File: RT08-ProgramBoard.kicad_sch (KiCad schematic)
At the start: 5 parts, among them J1 PWR/Addr, J2 Instruction, J3 Data, J4 Instruction, J5 Data

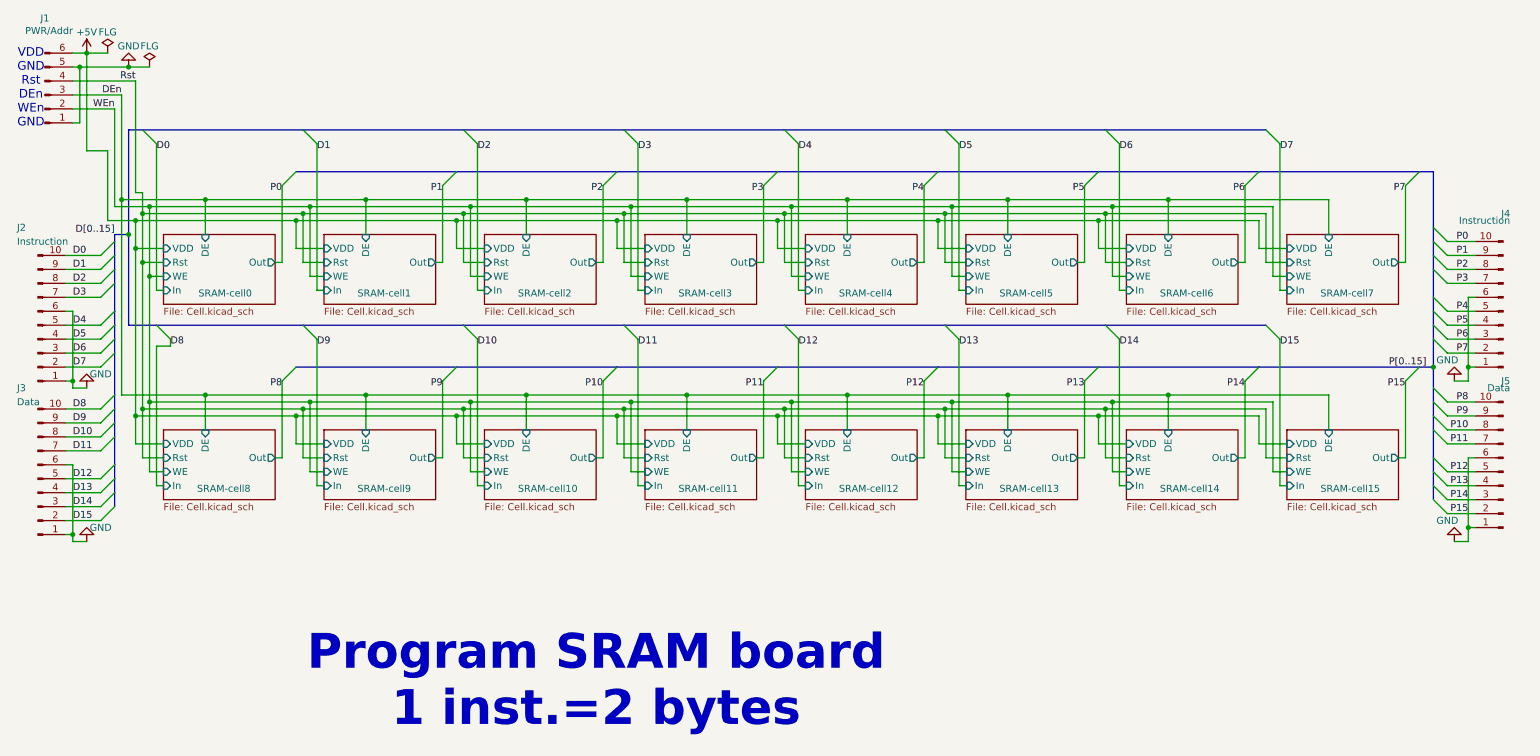
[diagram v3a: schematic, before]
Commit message: Deleted '-' from its name, officially
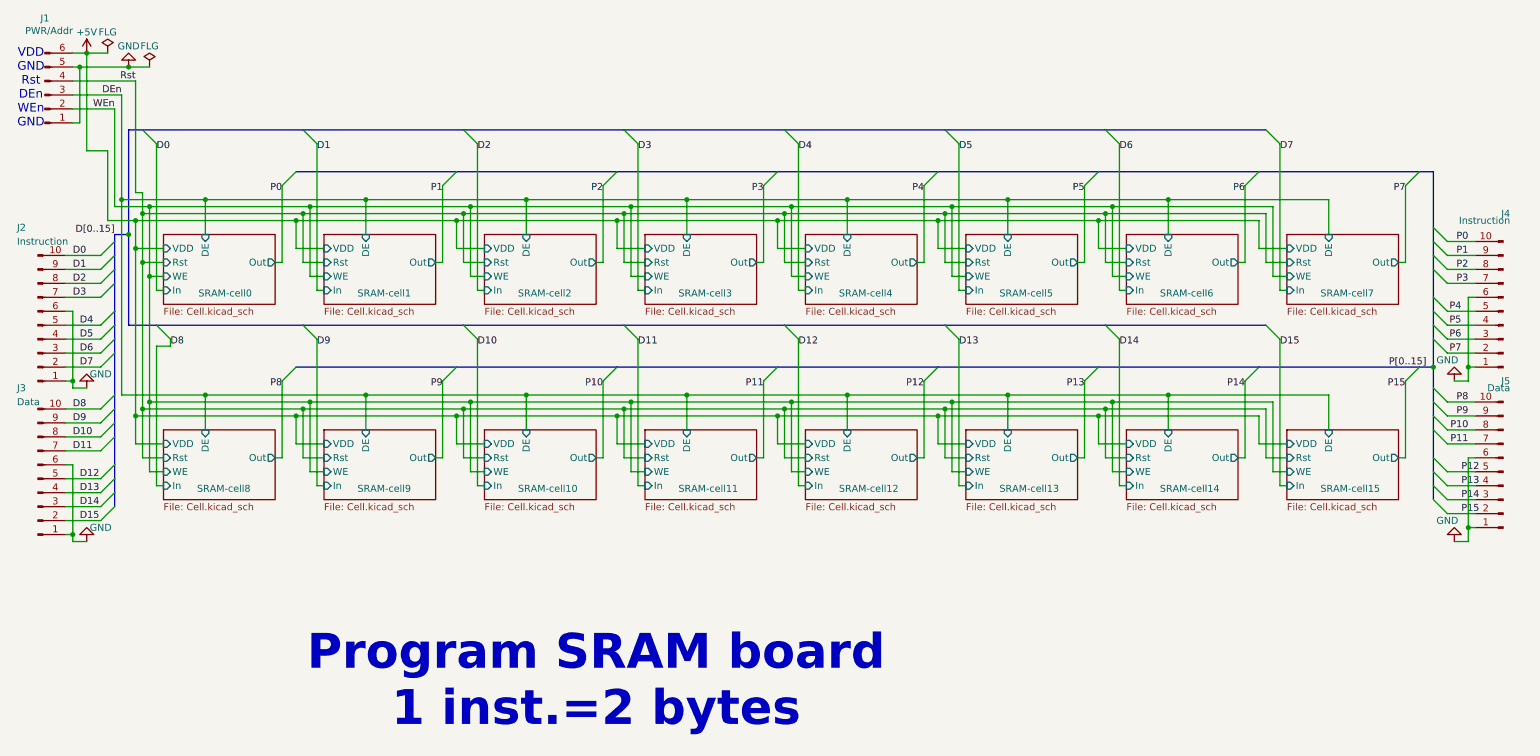
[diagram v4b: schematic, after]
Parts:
- J5: footprint Connector_PinHeader_2.54mm:PinHeader_1x08_P2.54mm_Horizontal -> Connector_PinHeader_2.54mm:PinHeader_1x10_P2.54mm_Horizontal
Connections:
- net GND: no longer J2.2 (Pin_2), J2.3 (Pin_3), J2.4 (Pin_4), J2.5 (Pin_5), J3.2 (Pin_2), J3.3 (Pin_3), J3.4 (Pin_4), J3.5 (Pin_5), J4.2 (Pin_2), J4.3 (Pin_3), J4.4 (Pin_4), J4.5 (Pin_5), J5.2 (Pin_2), J5.3 (Pin_3), J5.4 (Pin_4), J5.5 (Pin_5)
- new net D12: J3.5 (Pin_5)
- new net D13: J3.4 (Pin_4)
- new net D14: J3.3 (Pin_3)
- new net D15: J3.2 (Pin_2)
- new net D4: J2.5 (Pin_5)
- new net D5: J2.4 (Pin_4)
- new net D6: J2.3 (Pin_3)
- new net D7: J2.2 (Pin_2)
- new net P12: J5.5 (Pin_5)
- new net P13: J5.4 (Pin_4)
- new net P14: J5.3 (Pin_3)
- new net P15: J5.2 (Pin_2)
- new net P4: J4.5 (Pin_5)
- new net P5: J4.4 (Pin_4)
- new net P6: J4.3 (Pin_3)
- new net P7: J4.2 (Pin_2)
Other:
- title: Y-tran RT-08 Program board -> Y-tran RT08 Program board
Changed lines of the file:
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@@
 	(paper "A4")
 	(title_block
-		(title "Y-tran RT-08 Program board")
+		(title "Y-tran RT08 Program board")
 		(date "2025/3~5")
 		(rev "C")
@@
 		)
 	)
-	(wire
-		(pts
-			(xy 21.59 120.65) (xy 27.94 120.65)
-		)
-		(stroke
-			(width 0)
-			(type default)
-		)
-	)
 	(bus
 		(pts
@@
 	(wire
 		(pts
+			(xy 273.05 154.94) (xy 278.13 154.94)
+		)
+		(stroke
+			(width 0)
+			(type default)
+		)
+	)
+	(wire
+		(pts
 			(xy 66.04 134.62) (xy 95.25 134.62)
 		)
@@
 	(wire
 		(pts
+			(xy 273.05 120.65) (xy 278.13 120.65)
+		)
+		(stroke
+			(width 0)
+			(type default)
+		)
+	)
+	(wire
+		(pts
 			(xy 93.98 135.89) (xy 93.98 144.78)
 		)
@@
 	(wire
 		(pts
+			(xy 22.86 146.05) (xy 22.86 158.75)
+		)
+		(stroke
+			(width 0)
+			(type default)
+		)
+	)
+	(wire
+		(pts
 			(xy 123.19 144.78) (xy 127 144.78)
 		)
@@
 		)
 	)
+	(wire
+		(pts
+			(xy 276.86 144.78) (xy 276.86 157.48)
+		)
+		(stroke
+			(width 0)
+			(type default)
+		)
+	)
 	(bus
 		(pts
@@
 	(wire
 		(pts
-			(xy 21.59 123.19) (xy 27.94 123.19)
-		)
-		(stroke
-			(width 0)
-			(type default)
-		)
-	)
-	(wire
-		(pts
 			(xy 134.62 97.79) (xy 163.83 97.79)
 		)
@@
 	(wire
 		(pts
-			(xy 22.86 146.05) (xy 22.86 158.75)
-		)
-		(stroke
-			(width 0)
-			(type default)
-		)
-	)
-	(wire
-		(pts
 			(xy 205.74 144.78) (xy 207.01 144.78)
 		)
@@
 	(wire
 		(pts
+			(xy 276.86 115.57) (xy 276.86 128.27)
+		)
+		(stroke
+			(width 0)
+			(type default)
+		)
+	)
+	(wire
+		(pts
 			(xy 22.86 83.82) (xy 24.13 83.82)
 		)
@@
 	(wire
 		(pts
+			(xy 21.59 123.19) (xy 27.94 123.19)
+		)
+		(stroke
+			(width 0)
+			(type default)
+		)
+	)
+	(wire
+		(pts
 			(xy 36.83 111.76) (xy 36.83 134.62)
 		)
@@
 	(wire
 		(pts
-			(xy 273.05 154.94) (xy 278.13 154.94)
-		)
-		(stroke
-			(width 0)
-			(type default)
-		)
-	)
-	(wire
-		(pts
 			(xy 21.59 140.97) (xy 27.94 140.97)
 		)
@@
 	(wire
 		(pts
-			(xy 276.86 115.57) (xy 276.86 128.27)
-		)
-		(stroke
-			(width 0)
-			(type default)
-		)
-	)
-	(wire
-		(pts
 			(xy 147.32 109.22) (xy 148.59 109.22)
 		)
@@
 	(wire
 		(pts
-			(xy 181.61 100.33) (xy 210.82 100.33)
+			(xy 22.86 118.11) (xy 22.86 130.81)
 		)
 		(stroke
@@
 	(wire
 		(pts
-			(xy 105.41 97.79) (xy 105.41 104.14)
+			(xy 181.61 100.33) (xy 210.82 100.33)
 		)
 		(stroke
@@
 	(wire
 		(pts
-			(xy 210.82 100.33) (xy 210.82 109.22)
+			(xy 105.41 97.79) (xy 105.41 104.14)
 		)
 		(stroke
@@
 	(wire
 		(pts
-			(xy 63.5 142.24) (xy 68.58 142.24)
+			(xy 210.82 100.33) (xy 210.82 109.22)
 		)
 		(stroke
@@
 	(wire
 		(pts
-			(xy 21.59 151.13) (xy 27.94 151.13)
+			(xy 63.5 142.24) (xy 68.58 142.24)
 		)
 		(stroke
@@
 	(wire
 		(pts
+			(xy 21.59 151.13) (xy 27.94 151.13)
+		)
+		(stroke
+			(width 0)
+			(type default)
+		)
+	)
+	(wire
+		(pts
 			(xy 240.03 144.78) (xy 243.84 144.78)
 		)
@@
 	(wire
 		(pts
+			(xy 21.59 128.27) (xy 27.94 128.27)
+		)
+		(stroke
+			(width 0)
+			(type default)
+		)
+	)
+	(wire
+		(pts
 			(xy 163.83 97.79) (xy 163.83 104.14)
 		)
@@
 	(wire
 		(pts
-			(xy 21.59 128.27) (xy 27.94 128.27)
+			(xy 34.29 142.24) (xy 39.37 142.24)
 		)
 		(stroke
@@
 	(wire
 		(pts
-			(xy 34.29 142.24) (xy 39.37 142.24)
+			(xy 21.59 125.73) (xy 27.94 125.73)
 		)
 		(stroke
@@
 	(wire
 		(pts
-			(xy 273.05 137.16) (xy 278.13 137.16)
+			(xy 21.59 120.65) (xy 27.94 120.65)
 		)
 		(stroke
@@
 	(wire
 		(pts
-			(xy 30.48 81.28) (xy 30.48 99.06)
+			(xy 273.05 137.16) (xy 278.13 137.16)
 		)
 		(stroke
@@
 		)
 	)
-	(bus
+	(wire
 		(pts
-			(xy 30.48 140.97) (xy 30.48 146.05)
+			(xy 30.48 81.28) (xy 30.48 99.06)
 		)
 		(stroke
@@
 		)
 	)
-	(wire
+	(bus
 		(pts
-			(xy 21.59 125.73) (xy 27.94 125.73)
+			(xy 30.48 140.97) (xy 30.48 146.05)
 		)
 		(stroke
@@
 		)
 	)
-	(wire
-		(pts
-			(xy 273.05 120.65) (xy 278.13 120.65)
-		)
-		(stroke
-			(width 0)
-			(type default)
-		)
-	)
 	(bus
 		(pts
@@
 	(wire
 		(pts
-			(xy 22.86 118.11) (xy 22.86 130.81)
-		)
-		(stroke
-			(width 0)
-			(type default)
-		)
-	)
-	(wire
-		(pts
-			(xy 276.86 144.78) (xy 276.86 157.48)
-		)
-		(stroke
-			(width 0)
-			(type default)
-		)
-	)
-	(wire
-		(pts
 			(xy 92.71 106.68) (xy 97.79 106.68)
 		)
@@
 	)
 	(label "D14"
-		(at 22.86 153.67 0)
+		(at 24.13 153.67 0)
 		(effects
 			(font
@@
 	)
 	(label "D15"
-		(at 22.86 156.21 0)
+		(at 24.13 156.21 0)
 		(effects
 			(font
@@
 	)
 	(label "P12"
-		(at 276.86 147.32 180)
+		(at 275.59 147.32 0)
 		(effects
 			(font
 				(size 1.27 1.27)
 			)
-			(justify right bottom)
+			(justify left bottom)
 		)
 	)
@@
 	)
 	(label "P7"
-		(at 276.86 125.73 180)
+		(at 275.59 125.73 180)
 		(effects
 			(font
@@
 	)
 	(label "D4"
-		(at 22.86 120.65 0)
+		(at 24.13 120.65 0)
 		(effects
 			(font
@@
 	)
 	(label "D5"
-		(at 22.86 123.19 0)
+		(at 24.13 123.19 0)
 		(effects
 			(font
@@
 	)
 	(label "D7"
-		(at 22.86 128.27 0)
+		(at 24.13 128.27 0)
 		(effects
 			(font
@@
 	)
 	(label "D13"
-		(at 22.86 151.13 0)
+		(at 24.13 151.13 0)
 		(effects
 			(font
@@
 	)
 	(label "P6"
-		(at 276.86 123.19 180)
+		(at 275.59 123.19 180)
 		(effects
 			(font
@@
 	)
 	(label "P15"
-		(at 276.86 154.94 180)
+		(at 275.59 154.94 0)
 		(effects
 			(font
 				(size 1.27 1.27)
 			)
-			(justify right bottom)
+			(justify left bottom)
 		)
 	)
 	(label "P4"
-		(at 276.86 118.11 180)
+		(at 275.59 118.11 180)
 		(effects
 			(font
@@
 	)
 	(label "P14"
-		(at 276.86 152.4 180)
+		(at 275.59 152.4 0)
 		(effects
 			(font
 				(size 1.27 1.27)
 			)
-			(justify right bottom)
+			(justify left bottom)
 		)
 	)
@@
 	)
 	(label "D6"
-		(at 22.86 125.73 0)
+		(at 24.13 125.73 0)
 		(effects
 			(font
@@
 	)
 	(label "P5"
-		(at 276.86 120.65 180)
+		(at 275.59 120.65 180)
 		(effects
 			(font
@@
 	)
 	(label "D12"
-		(at 22.86 148.59 0)
+		(at 24.13 148.59 0)
 		(effects
 			(font
@@
 	)
 	(label "P13"
-		(at 276.86 149.86 180)
+		(at 275.59 149.86 0)
 		(effects
 			(font
 				(size 1.27 1.27)
 			)
-			(justify right bottom)
+			(justify left bottom)
 		)
 	)
@@
 			)
 		)
-		(property "Footprint" "Connector_PinHeader_2.54mm:PinHeader_1x08_P2.54mm_Horizontal"
+		(property "Footprint" "Connector_PinHeader_2.54mm:PinHeader_1x10_P2.54mm_Horizontal"
 			(at 283.21 147.32 0)
 			(effects

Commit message: Updated pinouts n' something
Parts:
- removed J3, J5: Data, Connector_PinHeader_2.54mm:PinHeader_1x10_P2.54mm_Horizontal, symbol Connector:Conn_01x10_Pin
- removed J4: Instruction, Connector_PinHeader_2.54mm:PinHeader_1x10_P2.54mm_Horizontal, symbol Connector:Conn_01x10_Pin
- added J3, J7: Inst-2, Connector_PinHeader_2.54mm:PinHeader_1x06_P2.54mm_Horizontal, symbol Connector:Conn_01x06_Pin
- added J4, J8: Data-1, Connector_PinHeader_2.54mm:PinHeader_1x06_P2.54mm_Horizontal, symbol Connector:Conn_01x06_Pin
- added J5, J9: Data-2, Connector_PinHeader_2.54mm:PinHeader_1x06_P2.54mm_Horizontal, symbol Connector:Conn_01x06_Pin
- added J6: Inst-1, Connector_PinHeader_2.54mm:PinHeader_1x06_P2.54mm_Horizontal, symbol Connector:Conn_01x06_Pin
- J2: value Instruction -> Inst-1; footprint Connector_PinHeader_2.54mm:PinHeader_1x10_P2.54mm_Horizontal -> Connector_PinHeader_2.54mm:PinHeader_1x06_P2.54mm_Horizontal; symbol Connector:Conn_01x10_Pin -> Connector:Conn_01x06_Pin
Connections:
- net D0: now also J2.6 (Pin_6); no longer J2.10 (Pin_10)
- net D1: now also J2.5 (Pin_5); no longer J2.9 (Pin_9)
- net D10: now also J4.3 (Pin_3)
- net D11: now also J4.2 (Pin_2)
- net D12: now also J5.6 (Pin_6)
- net D13: now also J5.5 (Pin_5)
- net D14: now also J5.3 (Pin_3)
- net D15: now also J5.2 (Pin_2)
- net D2: now also J2.3 (Pin_3); no longer J2.8 (Pin_8)
- net D3: now also J2.2 (Pin_2); no longer J2.7 (Pin_7)
- net D4: now also J3.6 (Pin_6); no longer J2.5 (Pin_5)
- net D5: now also J3.5 (Pin_5); no longer J2.4 (Pin_4)
- net D6: now also J3.3 (Pin_3); no longer J2.3 (Pin_3)
- net D7: now also J3.2 (Pin_2); no longer J2.2 (Pin_2)
- net D8: now also J4.6 (Pin_6)
- net D9: now also J4.5 (Pin_5)
- net GND: now also J2.4 (Pin_4), J3.1 (Pin_1), J3.4 (Pin_4), J4.1 (Pin_1), J4.4 (Pin_4), J5.1 (Pin_1), J5.4 (Pin_4), J6.1 (Pin_1), J6.4 (Pin_4), J7.1 (Pin_1), J7.4 (Pin_4), J8.1 (Pin_1), J8.4 (Pin_4), J9.1 (Pin_1), J9.4 (Pin_4); no longer J2.6 (Pin_6)
- net P0: now also J6.6 (Pin_6)
- net P1: now also J6.5 (Pin_5)
- net P10: now also J8.3 (Pin_3)
- net P11: now also J8.2 (Pin_2)
- net P12: now also J9.6 (Pin_6)
- net P13: now also J9.5 (Pin_5)
- net P14: now also J9.3 (Pin_3)
- net P15: now also J9.2 (Pin_2)
- net P2: now also J6.3 (Pin_3)
- net P3: now also J6.2 (Pin_2)
- net P4: now also J7.6 (Pin_6)
- net P5: now also J7.5 (Pin_5)
- net P6: now also J7.3 (Pin_3)
- net P7: now also J7.2 (Pin_2)
- net P8: now also J8.6 (Pin_6)
- net P9: now also J8.5 (Pin_5)

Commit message: Changed pinheaders
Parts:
- J1, J2, J3, J4, J5, J6, J7, J8, J9: footprint Connector_PinHeader_2.54mm:PinHeader_1x06_P2.54mm_Horizontal -> Connector_PinHeader_2.54mm:PinHeader_1x06_P2.54mm_Vertical
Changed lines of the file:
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@@
 			)
 		)
-		(property "Footprint" "Connector_PinHeader_2.54mm:PinHeader_1x06_P2.54mm_Horizontal"
+		(property "Footprint" "Connector_PinHeader_2.54mm:PinHeader_1x06_P2.54mm_Vertical"
 			(at 283.21 157.48 0)
 			(effects
@@
 			)
 		)
-		(property "Footprint" "Connector_PinHeader_2.54mm:PinHeader_1x06_P2.54mm_Horizontal"
+		(property "Footprint" "Connector_PinHeader_2.54mm:PinHeader_1x06_P2.54mm_Vertical"
 			(at 15.24 133.35 0)
 			(effects
@@
 			)
 		)
-		(property "Footprint" "Connector_PinHeader_2.54mm:PinHeader_1x06_P2.54mm_Horizontal"
+		(property "Footprint" "Connector_PinHeader_2.54mm:PinHeader_1x06_P2.54mm_Vertical"
 			(at 283.21 104.14 0)
 			(effects
@@
 			)
 		)
-		(property "Footprint" "Connector_PinHeader_2.54mm:PinHeader_1x06_P2.54mm_Horizontal"
+		(property "Footprint" "Connector_PinHeader_2.54mm:PinHeader_1x06_P2.54mm_Vertical"
 			(at 15.24 151.13 0)
 			(effects
@@
 			)
 		)
-		(property "Footprint" "Connector_PinHeader_2.54mm:PinHeader_1x06_P2.54mm_Horizontal"
+		(property "Footprint" "Connector_PinHeader_2.54mm:PinHeader_1x06_P2.54mm_Vertical"
 			(at 15.24 115.57 0)
 			(effects
@@
 			)
 		)
-		(property "Footprint" "Connector_PinHeader_2.54mm:PinHeader_1x06_P2.54mm_Horizontal"
+		(property "Footprint" "Connector_PinHeader_2.54mm:PinHeader_1x06_P2.54mm_Vertical"
 			(at 15.24 168.91 0)
 			(effects
@@
 			)
 		)
-		(property "Footprint" "Connector_PinHeader_2.54mm:PinHeader_1x06_P2.54mm_Horizontal"
+		(property "Footprint" "Connector_PinHeader_2.54mm:PinHeader_1x06_P2.54mm_Vertical"
 			(at 283.21 139.7 0)
 			(effects
@@
 			)
 		)
-		(property "Footprint" "Connector_PinHeader_2.54mm:PinHeader_1x06_P2.54mm_Horizontal"
+		(property "Footprint" "Connector_PinHeader_2.54mm:PinHeader_1x06_P2.54mm_Vertical"
 			(at 17.78 78.74 0)
 			(effects
@@
 			)
 		)
-		(property "Footprint" "Connector_PinHeader_2.54mm:PinHeader_1x06_P2.54mm_Horizontal"
+		(property "Footprint" "Connector_PinHeader_2.54mm:PinHeader_1x06_P2.54mm_Vertical"
 			(at 283.21 121.92 0)
 			(effects

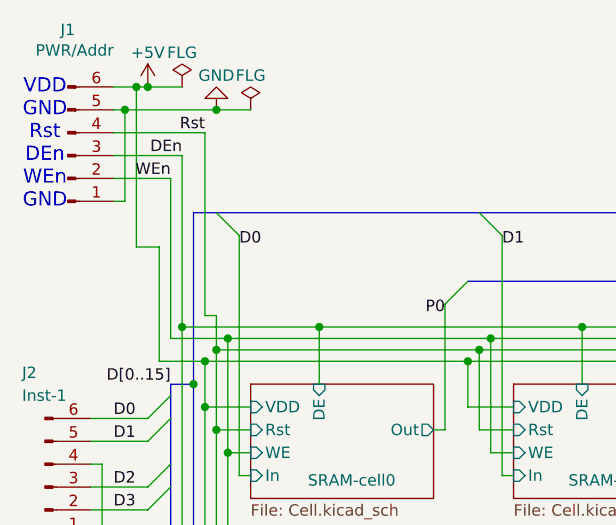
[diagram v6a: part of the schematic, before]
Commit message: Adding one more parts per bit, editing PCB
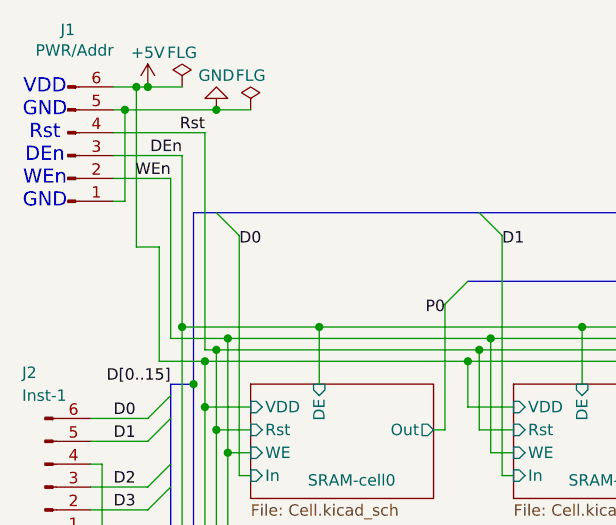
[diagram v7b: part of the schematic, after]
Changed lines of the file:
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@@
 		(title "Y-tran RT08 Program board")
 		(date "2025/3~8")
-		(rev "D")
+		(rev "E")
 		(company "@7654jp")
 		(comment 2 "to provide instructions.")
@@
 	(wire
 		(pts
-			(xy 33.02 96.52) (xy 34.29 96.52)
-		)
-		(stroke
-			(width 0)
-			(type default)
-		)
-	)
-	(wire
-		(pts
 			(xy 95.25 87.63) (xy 95.25 114.3)
 		)
@@
 	(wire
 		(pts
-			(xy 34.29 96.52) (xy 34.29 100.33)
-		)
-		(stroke
-			(width 0)
-			(type default)
-		)
-	)
-	(wire
-		(pts
 			(xy 220.98 133.35) (xy 250.19 133.35)
 		)
@@
 	(wire
 		(pts
-			(xy 33.02 76.2) (xy 33.02 96.52)
+			(xy 33.02 76.2) (xy 33.02 100.33)
 		)
 		(stroke
@@
 		)
 		(stroke
+			(width 0)
+			(type default)
+		)
+	)
+	(wire
+		(pts
+			(xy 33.02 100.33) (xy 34.29 100.33)
+		)
+		(stroke
